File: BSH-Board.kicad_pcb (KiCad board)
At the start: 2 copper layers, 20 x 28.5 mm, 14 parts, among them J1 667101210103, U1 ESP32-S2-MINI-2-N4, U2 TPSM863257RDXR, U3 TXS0102DQER, U5 AP63203WU

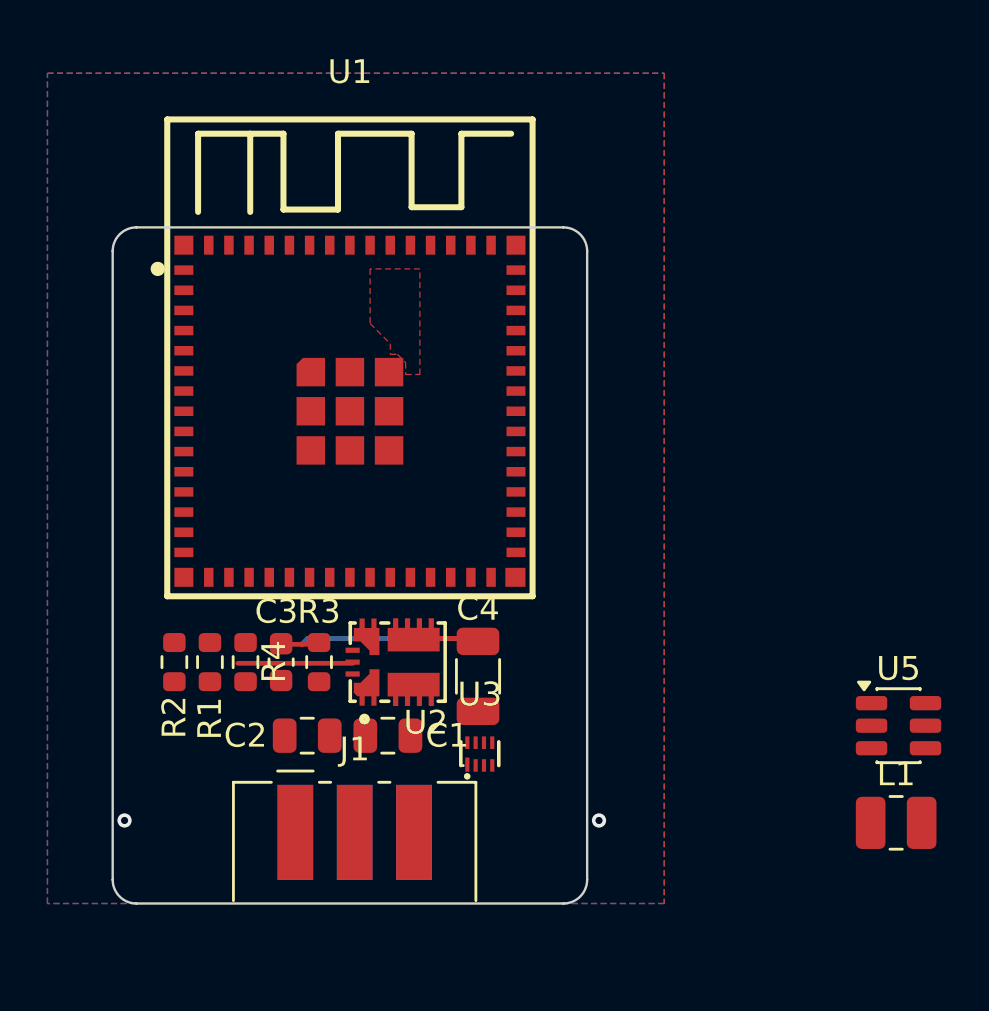
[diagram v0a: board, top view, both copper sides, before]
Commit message: Add LDO for 5V
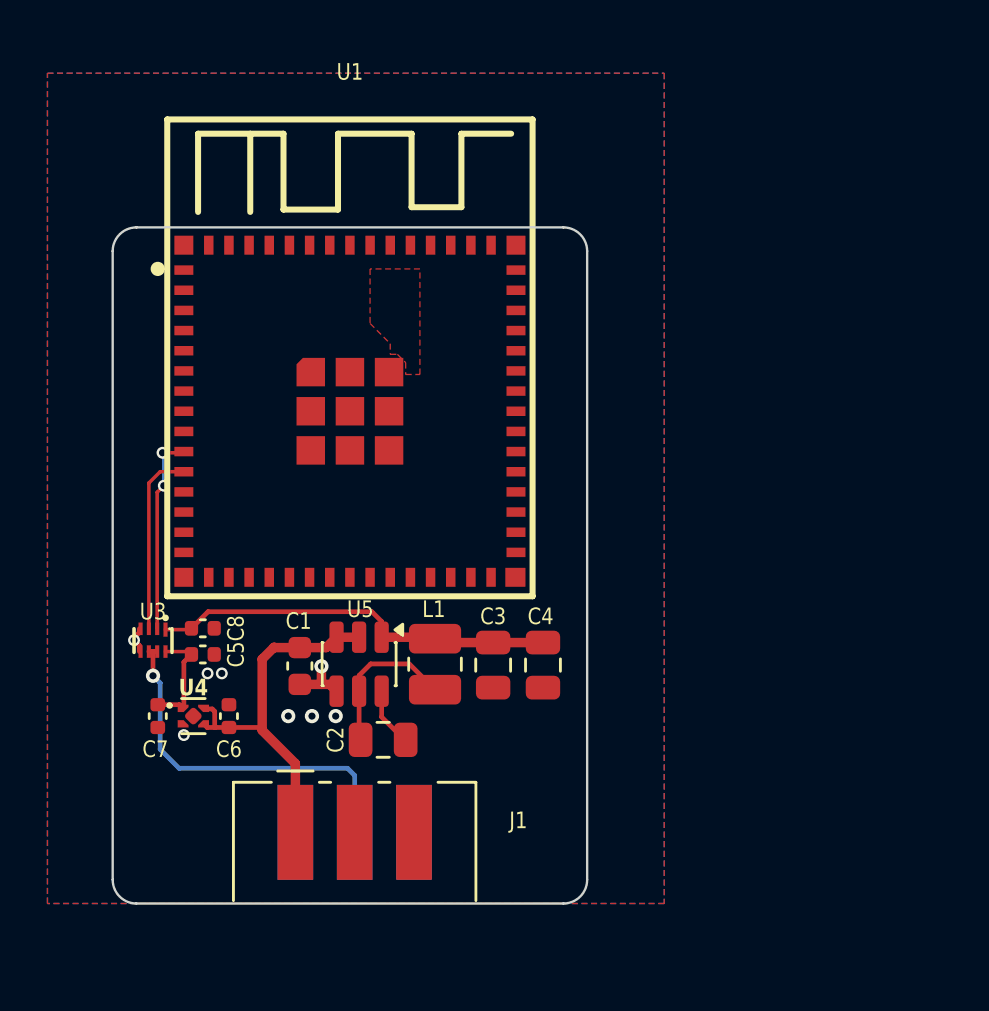
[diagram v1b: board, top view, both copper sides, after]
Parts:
- removed R1: 62k, Resistor_SMD:R_0603_1608Metric
- removed R2, R4: 30k, Resistor_SMD:R_0603_1608Metric
- removed R3: 220k, Resistor_SMD:R_0603_1608Metric
- removed U2: TPSM863257RDXR, footprints:QFN-7_L4.0-W3.3_TPSM863257RDXR
- added C5: 100nF, Capacitor_SMD:C_0402_1005Metric, F.Cu at (115.8, 78.0)
- added C6: 1uF, Capacitor_SMD:C_0402_1005Metric, F.Cu at (116.9, 80.6)
- added C7: 1uF, Capacitor_SMD:C_0402_1005Metric, F.Cu at (113.9, 80.6)
- added C8: 100nF, Capacitor_SMD:C_0402_1005Metric, F.Cu at (115.8, 76.9)
- added U4: TPS7A2050PDQNR, Package_SON:Texas_X2SON-4_1x1mm_P0.65mm, F.Cu at (115.4, 80.6)
- C1: footprint Capacitor_SMD:C_0805_2012Metric -> Capacitor_SMD:C_0603_1608Metric
- C3: value 22pF -> 22uF; footprint Capacitor_SMD:C_0603_1608Metric -> Capacitor_SMD:C_0805_2012Metric
- C4: footprint Capacitor_SMD:C_1206_3216Metric -> Capacitor_SMD:C_0805_2012Metric
- L1: value L_Small -> 4.7uH
- moved U5 22.9 mm to (122.4, 78.4), turned to -90 degrees
- moved L1 20.6 mm to (125.6, 78.4), turned to 90 degrees
- moved U3 14.6 mm to (113.7, 77.4), turned to 180 degrees
- moved C3 8.94 mm to (128.0, 78.5)
- moved C1 4.73 mm to (119.9, 78.5), turned to -90 degrees
- moved C2 3.20 mm to (123.4, 81.6), turned to 0 degrees
- moved C4 2.78 mm to (130.1, 78.5)
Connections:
- C2 pad 1: VCC -> Net-(U5-SW)
- C2 pad 2: GND -> Net-(U5-BST)
- C3 pad 1: +5V -> +3.3V
- C3 pad 2: /FB -> GND
- C4 pad 1: +5V -> +3.3V
- L1 pad 1: unconnected-(L1-Pad1) -> Net-(U5-SW)
- L1 pad 2: unconnected-(L1-Pad2) -> +3.3V
- U1 pad 1: unconnected-(U1-GND-Pad1) -> GND
- U1 pad 10: unconnected-(U1-IO6-Pad10) -> A1
- U1 pad 11: unconnected-(U1-IO7-Pad11) -> A2
- U1 pad 2: unconnected-(U1-GND-Pad2) -> GND
- U1 pad 3: unconnected-(U1-3V3-Pad3) -> +3.3V
- U1 pad 30: unconnected-(U1-GND-Pad30) -> GND
- U1 pad 42: unconnected-(U1-GND-Pad42) -> GND
- U1 pad 43: unconnected-(U1-GND-Pad43) -> GND
- U1 pad 46: unconnected-(U1-GND-Pad46) -> GND
- U1 pad 47: unconnected-(U1-GND-Pad47) -> GND
- U1 pad 48: unconnected-(U1-GND-Pad48) -> GND
- U1 pad 49: unconnected-(U1-GND-Pad49) -> GND
- U1 pad 50: unconnected-(U1-GND-Pad50) -> GND
- U1 pad 51: unconnected-(U1-GND-Pad51) -> GND
- U1 pad 52: unconnected-(U1-GND-Pad52) -> GND
- U1 pad 53: unconnected-(U1-GND-Pad53) -> GND
- U1 pad 54: unconnected-(U1-GND-Pad54) -> GND
- U1 pad 55: unconnected-(U1-GND-Pad55) -> GND
- U1 pad 56: unconnected-(U1-GND-Pad56) -> GND
- U1 pad 57: unconnected-(U1-GND-Pad57) -> GND
- U1 pad 58: unconnected-(U1-GND-Pad58) -> GND
- U1 pad 59: unconnected-(U1-GND-Pad59) -> GND
- U1 pad 60: unconnected-(U1-GND-Pad60) -> GND
- U1 pad 61: unconnected-(U1-GND-Pad61) -> GND
- U1 pad 62: unconnected-(U1-GND-Pad62) -> GND
- U1 pad 63: unconnected-(U1-GND-Pad63) -> GND
- U1 pad 64: unconnected-(U1-GND-Pad64) -> GND
- U1 pad 9: D-BUS -> unconnected-(U1-IO5-Pad9)
- U3 pad 1: unconnected-(U3-VCCA-Pad1) -> +3.3V
- U3 pad 2: unconnected-(U3-A1-Pad2) -> A1
- U3 pad 3: unconnected-(U3-A2-Pad3) -> A2
- U3 pad 4: unconnected-(U3-GND-Pad4) -> GND
- U3 pad 5: unconnected-(U3-OE-Pad5) -> GND
- U3 pad 6: unconnected-(U3-B2-Pad6) -> D-BUS
- U3 pad 7: unconnected-(U3-B1-Pad7) -> D-BUS
- U3 pad 8: unconnected-(U3-VCCB-Pad8) -> +5V
- U5 pad 1: unconnected-(U5-FB-Pad1) -> +3.3V
- U5 pad 2: unconnected-(U5-EN-Pad2) -> VCC
- U5 pad 3: unconnected-(U5-IN-Pad3) -> VCC
- U5 pad 4: unconnected-(U5-GND-Pad4) -> GND
- U5 pad 5: unconnected-(U5-SW-Pad5) -> Net-(U5-SW)
- U5 pad 6: unconnected-(U5-BST-Pad6) -> Net-(U5-BST)
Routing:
- net +3.3V: track 0.00 -> 17.2 mm
- net VCC: track 0.00 -> 16.1 mm
- net D-BUS: track 0.00 -> 15.6 mm, vias 0 -> 1
- net A1: track 0.00 -> 8.48 mm, vias 0 -> 2
- net A2: track 0.00 -> 7.82 mm
- net Net-(U5-SW): track 0.00 -> 6.59 mm
- net +5V: track 9.99 -> 4.62 mm
- net /EN: track 4.86 -> 0.00 mm
- net GND: track 0.00 -> 3.58 mm, vias 2 -> 8
- net Net-(U5-BST): track 0.00 -> 2.50 mm

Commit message: Added USB, replaced various parts
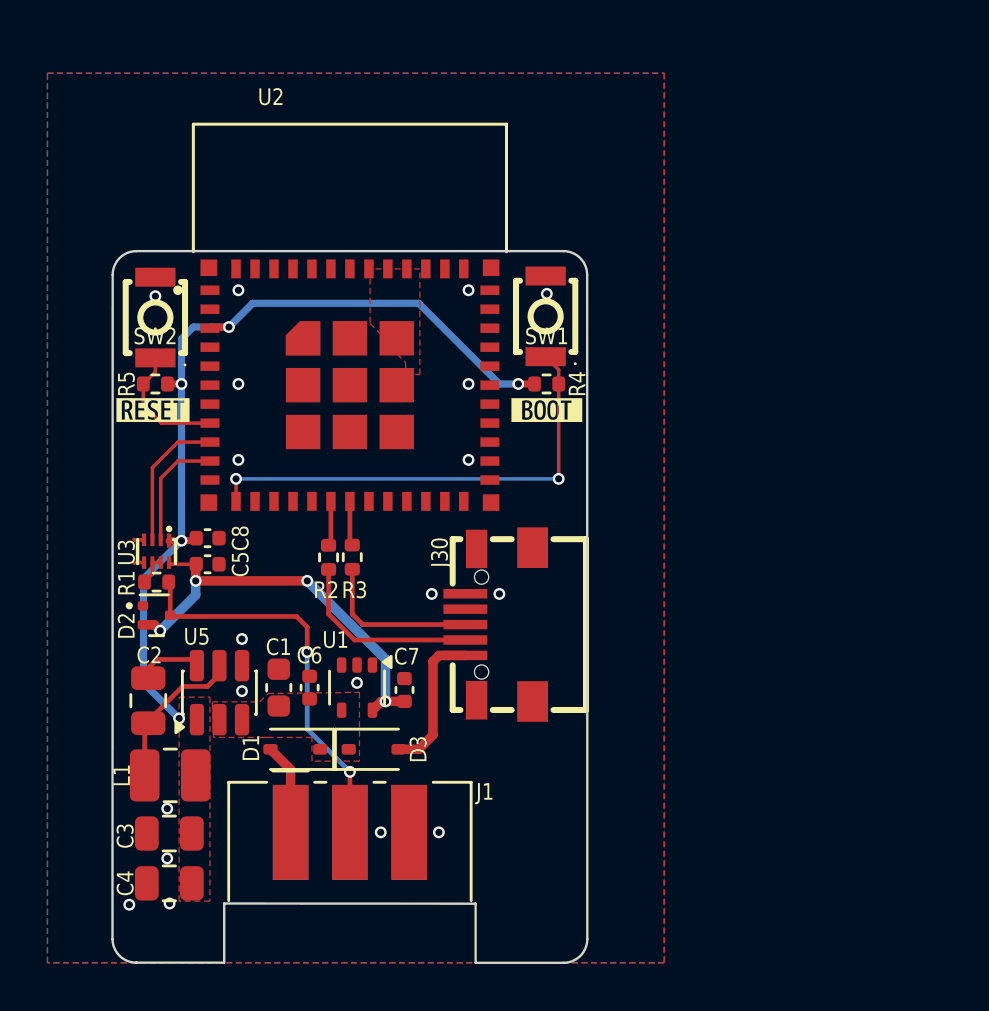
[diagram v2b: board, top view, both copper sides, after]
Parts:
- removed U4: TPS7A2050PDQNR, Package_SON:Texas_X2SON-4_1x1mm_P0.65mm
- added D1: BAT760,115, Diode_SMD:D_SOD-323, F.Cu at (119.7, 82.0)
- added D2: 1SS362FV,L3F, Package_TO_SOT_SMD:SOT-723, F.Cu at (113.8, 76.3)
- added D3: BAT760,115, Diode_SMD:D_SOD-323, F.Cu at (123.0, 82.0)
- added J30: MICRO QTZB5.0, footprints:MICRO-USB-SMD_MICRO-QTZB5.0, F.Cu at (128.3, 76.7)
- added R1: 150, Resistor_SMD:R_0402_1005Metric, F.Cu at (113.8, 75.0)
- added R2: 22, Resistor_SMD:R_0402_1005Metric, F.Cu at (121.1, 73.9)
- added R3: 22, Resistor_SMD:R_0402_1005Metric, F.Cu at (122.1, 73.9)
- added R4: 10k, Resistor_SMD:R_0402_1005Metric, F.Cu at (130.3, 66.6)
- added R5: 10k, Resistor_SMD:R_0402_1005Metric, F.Cu at (113.8, 66.6)
- added SW1: TS-3025-B-C-B, footprints:SW-SMD_L3.0-W2.5-P3.40-LS4.0-L, F.Cu at (130.2, 63.8)
- added SW2: TS-3025-B-C-B, footprints:SW-SMD_L3.0-W2.5-P3.40-LS4.0-L, F.Cu at (113.8, 63.8)
- added U2: ESP32-C6-MINI-1-N4, footprints:XCVR_ESP32-C6-MINI-1-N4, F.Cu at (122.0, 66.7)
- added kibuzzard-695BD43C: G***, kibuzzard-695BD43C, F.Cu at (113.7, 67.7)
- added kibuzzard-695BD459: G***, kibuzzard-695BD459, F.Cu at (130.3, 67.7)
- U1: value ESP32-S2-MINI-2-N4 -> NCP715SQ50T2G; footprint footprints:WIFI-SMD_ESP32-MINI-1-N4 -> Package_TO_SOT_SMD:SOT-353_SC-70-5
- moved C4 18.2 mm to (114.4, 87.7), turned to 180 degrees
- moved C3 15.4 mm to (114.4, 85.5), turned to 180 degrees
- moved L1 12.1 mm to (114.4, 83.1), turned to 0 degrees
- moved U1 11.7 mm to (122.3, 79.4), turned to -90 degrees
- moved C7 10.5 mm to (124.3, 79.5), turned to 90 degrees
- moved C2 10.0 mm to (113.5, 80.0), turned to 90 degrees
- moved U5 6.01 mm to (116.5, 79.6), turned to 90 degrees
- moved C8 3.81 mm to (116.0, 73.1)
- moved C5 3.81 mm to (116.0, 74.2)
- moved U3 3.75 mm to (113.8, 73.7)
- moved C6 3.61 mm to (120.3, 79.4)
- moved C1 1.27 mm to (119.0, 79.4), turned to 90 degrees
- moved J1 0.20 mm to (122.0, 85.5)
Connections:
- J1 pad A1: VCC -> Net-(D1-A)
- J1 pad B1: VCC -> Net-(D1-A)
- U1 pad 1: GND -> unconnected-(U1-NC-Pad1)
- U1 pad 3: +3.3V -> unconnected-(U1-NC-Pad3)
- U1 pad 4: unconnected-(U1-IO0-Pad4) -> VCC
- U1 pad 5: unconnected-(U1-IO1-Pad5) -> +5V
- U3 pad 2: A1 -> DBUS-RX
- U3 pad 3: A2 -> DBUS-TX
- U3 pad 6: D-BUS -> Net-(U3-B1)
- U3 pad 7: D-BUS -> Net-(U3-B1)
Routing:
- net BOOT: track 0.00 -> 19.9 mm, vias 0 -> 2
- net +3.3V: track 17.2 -> 36.8 mm, vias 0 -> 5
- net VCC: track 16.1 -> 0.00 mm
- net +5V: track 4.62 -> 18.1 mm, vias 0 -> 4
- net A1: track 8.48 -> 0.00 mm, vias 2 -> 0
- net USB-D-: track 0.00 -> 8.10 mm
- net A2: track 7.82 -> 0.00 mm
- net USB-D+: track 0.00 -> 6.84 mm
- net Net-(D3-A): track 0.00 -> 6.27 mm
- net DBUS-TX: track 0.00 -> 5.92 mm
- net RESET: track 0.00 -> 5.33 mm
- net DBUS-RX: track 0.00 -> 4.97 mm
- net Net-(D1-A): track 0.00 -> 3.85 mm
- net GND: track 3.58 -> 0.87 mm, vias 8 -> 19
- net Net-(U2-IO12): track 0.00 -> 1.89 mm
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- added copper zone on F.Cu, net +3.3V
- added copper zone on F.Cu, net VCC
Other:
- board size 20 x 28.5 mm -> 20 x 30 mm

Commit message: Added LCSC numbers, replaced parts with Basic parts, added LEDs
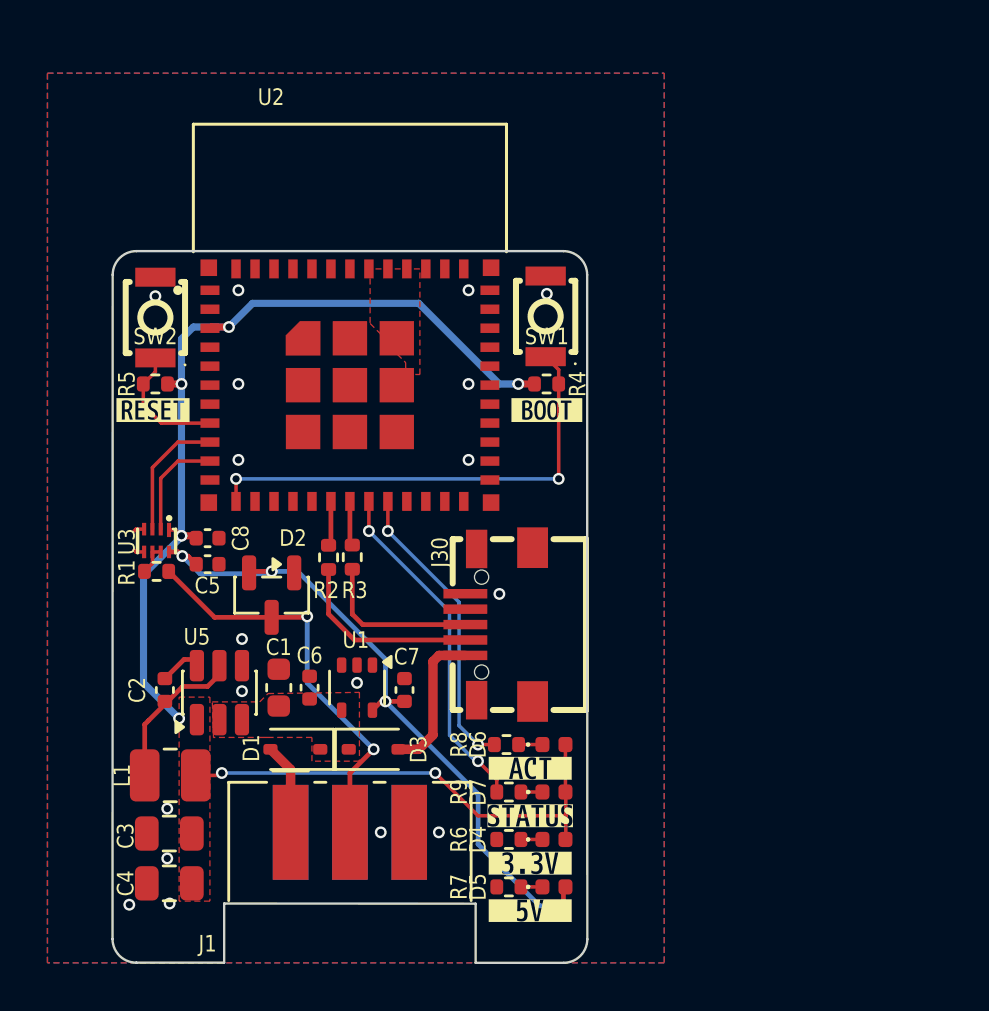
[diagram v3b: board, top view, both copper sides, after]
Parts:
- added D4: LED_R, LED_SMD:LED_0402_1005Metric, F.Cu at (130.6, 85.8)
- added D5: LED_G, LED_SMD:LED_0402_1005Metric, F.Cu at (130.6, 87.8)
- added D6: LED_B, LED_SMD:LED_0402_1005Metric, F.Cu at (130.6, 81.8)
- added D7: LED_Y, LED_SMD:LED_0402_1005Metric, F.Cu at (130.6, 83.8)
- added R6: 680, Resistor_SMD:R_0402_1005Metric, F.Cu at (128.7, 85.8)
- added R7: 330, Resistor_SMD:R_0402_1005Metric, F.Cu at (128.7, 87.8)
- added R8: 330, Resistor_SMD:R_0402_1005Metric, F.Cu at (128.6, 81.8)
- added R9: 680, Resistor_SMD:R_0402_1005Metric, F.Cu at (128.7, 83.8)
- added kibuzzard-695C20AA: G***, kibuzzard-695C20AA, F.Cu at (129.6, 84.8)
- added kibuzzard-695C20B0: G***, kibuzzard-695C20B0, F.Cu at (129.6, 86.8)
- added kibuzzard-695C20B7: G***, kibuzzard-695C20B7, F.Cu at (129.6, 88.8)
- added kibuzzard-695C20DE: G***, kibuzzard-695C20DE, F.Cu at (129.6, 82.8)
- C2: footprint Capacitor_SMD:C_0805_2012Metric -> Capacitor_SMD:C_0402_1005Metric
- D1, D3: value BAT760,115 -> 1N5819WS
- D2: value 1SS362FV,L3F -> BAV99,215; footprint Package_TO_SOT_SMD:SOT-723 -> Package_TO_SOT_SMD:SOT-23
- R1: value 150 -> 120
- moved D2 4.92 mm to (118.7, 75.5), turned to -90 degrees
- moved C2 0.83 mm to (114.2, 79.5)
- moved R1 0.45 mm to (113.8, 74.5)
- moved U3 0.45 mm to (113.8, 73.2)
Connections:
- U2 pad 19: unconnected-(U2-IO14-Pad19) -> STATUS
- U2 pad 20: unconnected-(U2-IO15-Pad20) -> ACTIVITY
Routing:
- net +3.3V: track 36.8 -> 57.3 mm, vias 5 -> 7
- net STATUS: track 0.00 -> 14.5 mm, vias 0 -> 2
- net ACTIVITY: track 0.00 -> 12.5 mm, vias 0 -> 2
- net +5V: track 18.1 -> 29.2 mm
- net Net-(D6-K): track 0.00 -> 1.00 mm
- net Net-(D7-K): track 0.00 -> 0.91 mm
- net Net-(D5-K): track 0.00 -> 0.91 mm
- net Net-(D4-K): track 0.00 -> 0.91 mm
- net Net-(U5-BST): track 2.53 -> 1.68 mm
- net GND: track 0.87 -> 0.92 mm, vias 19 -> 18

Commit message: Minor improvements
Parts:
- added kibuzzard-695CB6D3: G***, kibuzzard-695CB6D3, F.Cu at (119.5, 88.0)
- added kibuzzard-695CB6D3: G***, kibuzzard-695CB6D3, B.Cu at (119.5, 88.0)
- added kibuzzard-695CB704: G***, kibuzzard-695CB704, F.Cu at (122.0, 88.0)
- added kibuzzard-695CB704: G***, kibuzzard-695CB704, B.Cu at (122.0, 88.0)
- added kibuzzard-695CB724: G***, kibuzzard-695CB724, F.Cu at (124.5, 88.0)
- added kibuzzard-695CB724: G***, kibuzzard-695CB724, B.Cu at (124.5, 88.0)
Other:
- board text removed: "D-BUS"
- board text removed: "GND"
- board text removed: "VCC"

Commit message: Clenaupo
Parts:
- added C10: 100nF, Capacitor_SMD:C_0402_1005Metric, F.Cu at (113.8, 67.6)
- added C9: 100nF, Capacitor_SMD:C_0402_1005Metric, F.Cu at (130.3, 67.6)
- L1: value 4.7uH -> 3.3uH
- moved C8 2.64 mm to (113.4, 72.6), turned to 90 degrees
- moved C7 2.63 mm to (113.4, 74.6), turned to -90 degrees
- moved R1 1.07 mm to (114.8, 75.0)
- moved U4 1.03 mm to (114.8, 73.6), turned to 0 degrees
- moved kibuzzard-695BD43C 0.90 mm to (113.7, 68.6)
- moved kibuzzard-695BD459 0.90 mm to (130.3, 68.6)
- moved U1 0.15 mm to (122.0, 66.8)
- renumbered C6 to C5, C7 to C6, C5 to C7, D5 to D6, D4 to D7, D7 to D8, D6 to D9, J30 to J2, R7 to R6, R6 to R7, R9 to R8, R8 to R9, SW2 to SW1, SW1 to SW2, U2 to U1, U5 to U2, U1 to U3, U3 to U4
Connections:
- R1 pad 2: Net-(U3-B1) -> Net-(U4-A1)
- U1 pad 10: DBUS-RX -> DBUS-TX
- U1 pad 12: BOOT -> DBUS-ENABLE
- U1 pad 15: unconnected-(U2-IO6-Pad15) -> STATUS
- U1 pad 16: unconnected-(U2-IO7-Pad16) -> ACTIVITY
- U1 pad 19: STATUS -> unconnected-(U1-IO14-Pad19)
- U1 pad 20: ACTIVITY -> unconnected-(U1-IO15-Pad20)
- U1 pad 23: unconnected-(U2-IO9-Pad23) -> BOOT
- U1 pad 9: DBUS-TX -> DBUS-RX
- U4 pad 1: +3.3V -> +5V
- U4 pad 2: DBUS-RX -> Net-(U4-A1)
- U4 pad 3: DBUS-TX -> Net-(U4-A1)
- U4 pad 5: GND -> DBUS-ENABLE
- U4 pad 6: Net-(U3-B1) -> DBUS-TX
- U4 pad 7: Net-(U3-B1) -> DBUS-RX
- U4 pad 8: +5V -> +3.3V
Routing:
- net BOOT: track 19.9 -> 11.3 mm
- net STATUS: track 14.5 -> 17.6 mm
- net ACTIVITY: track 12.5 -> 15.6 mm
- net DBUS-ENABLE: track 0.00 -> 2.99 mm
- net DBUS-TX: track 5.47 -> 4.03 mm
- net Net-(U4-A1): track 0.00 -> 1.41 mm
- net D-BUS: track 17.3 -> 15.9 mm, vias 2 -> 3
- net Net-(U3-B1): track 1.28 -> 0.00 mm
- net +3.3V: track 57.3 -> 56.2 mm
- net +5V: track 29.2 -> 29.9 mm, vias 4 -> 3
- net DBUS-RX: track 4.52 -> 5.12 mm
- net GND: track 0.92 -> 0.62 mm, vias 18 -> 43
- net Net-(D1-A): vias 0 -> 1
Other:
- board text added: "${COMPANY}"
- board text added: "${TITLE}"
- board text added: "V${REVISION}"
